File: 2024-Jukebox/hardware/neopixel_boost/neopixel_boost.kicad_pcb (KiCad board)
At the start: 2 copper layers, 13 x 13 mm, 16 parts, among them J3 Conn_01x03, J4 Conn_01x03, Q1 BSS138, U1 TPS61090

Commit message: Minor updates to wand
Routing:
- removed copper zone on F.Cu, net GND
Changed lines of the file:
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@@
   (segment (start 3.1075 12.6325) (end 2.15 11.675) (width 0.25) (layer "F.Cu") (net 10))
   (segment (start 11.31 1.25) (end 11.31 3.5) (width 0.25) (layer "F.Cu") (net 10))
-  (zone (net 1) (net_name "GND") (layers "F&B.Cu") (hatch edge 0.5)
+  (zone (net 1) (net_name "GND") (layer "B.Cu") (hatch edge 0.5)
     (connect_pads (clearance 0.5))
     (min_thickness 0.25) (filled_areas_thickness no)

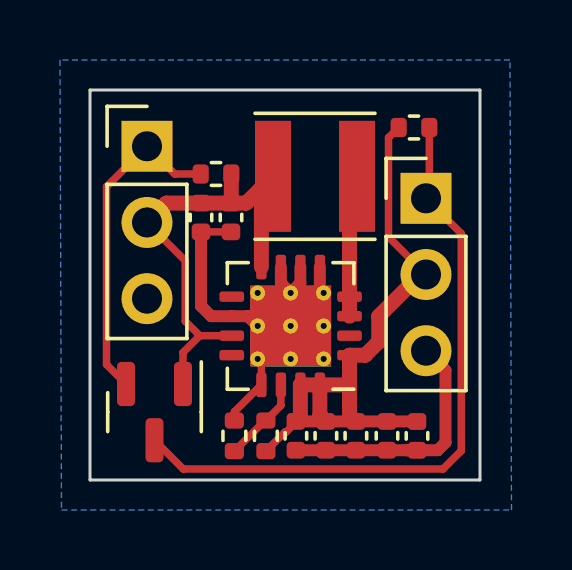
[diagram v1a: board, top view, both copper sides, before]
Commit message: Updates to neopixel circuit and ui board firmware
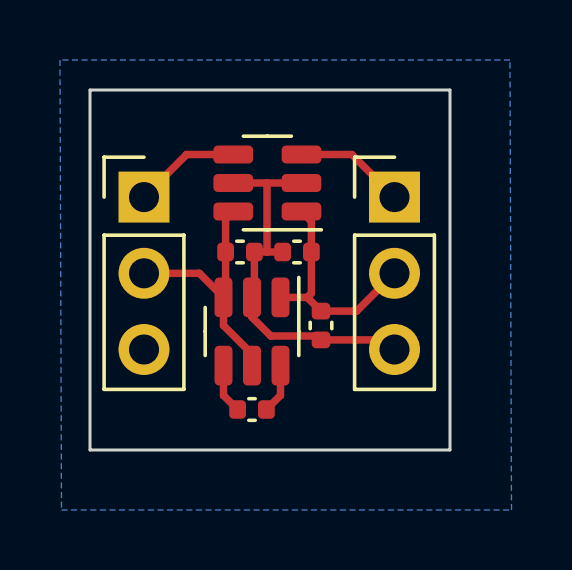
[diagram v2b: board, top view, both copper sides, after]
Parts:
- removed C3, C5, C6, C7: 10u, Capacitor_SMD:C_0402_1005Metric
- removed C4: 100n, Capacitor_SMD:C_0402_1005Metric
- removed L1: 6.8uH_1.0A_4018, Inductor_SMD:L_Taiyo-Yuden_NR-40xx
- removed Q1: BSS138, Package_TO_SOT_SMD:SOT-23
- removed R1: 1.8M, Resistor_SMD:R_0402_1005Metric
- removed R2: 200k, Resistor_SMD:R_0402_1005Metric
- removed R3, R4: 10k, Resistor_SMD:R_0402_1005Metric
- added C8: 1u, Capacitor_SMD:C_0402_1005Metric, F.Cu at (5.40, 10.7)
- added C9: 10u, Capacitor_SMD:C_0402_1005Metric, F.Cu at (5.00, 5.40)
- added U2: AP3602, Package_TO_SOT_SMD:SOT-23-6, F.Cu at (5.40, 8.05)
- C1: value 2.2u -> 10u
- C2: value 10u -> 100n
- U1: value TPS61090 -> SN74LVC1T45DBV; footprint Package_DFN_QFN:Texas_S-PVQFN-N16_EP2.7x2.7mm_ThermalVias -> Package_TO_SOT_SMD:SOT-23-6
- moved C1 6.13 mm to (6.90, 5.40), turned to 180 degrees
- moved U1 4.83 mm to (5.91, 3.10)
- moved C2 3.86 mm to (7.70, 7.85)
- moved J3 1.70 mm to (1.80, 3.57)
- moved J4 1.05 mm to (10.2, 3.57)
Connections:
- U1 pad 2: unconnected-(U1-NC-Pad2) -> GND
- U1 pad 3: Net-(L1-Pad2) -> Net-(J4-Pin_1)
- U1 pad 4: Net-(L1-Pad2) -> Net-(J3-Pin_1)
- U1 pad 6: GND -> +3V3
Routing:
- net Net-(J4-Pin_1): track 22.2 -> 3.69 mm
- net +5V: track 21.7 -> 7.57 mm
- net +3V3: track 17.2 -> 8.65 mm
- net Net-(J3-Pin_1): track 10.9 -> 3.56 mm
- net GND: track 19.8 -> 12.9 mm
- net Net-(L1-Pad2): track 4.77 -> 0.00 mm
- net Net-(U1-FB): track 2.87 -> 0.00 mm
- net Net-(U2-C-): track 0.00 -> 1.66 mm
- net Net-(U2-C+): track 0.00 -> 1.66 mm
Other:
- board size 13 x 13 mm -> 12 x 12 mm
